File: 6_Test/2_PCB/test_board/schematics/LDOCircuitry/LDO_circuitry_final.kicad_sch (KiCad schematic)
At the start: 6 parts

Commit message: Edits 112524
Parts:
- removed C? (x2): 4.7uF, symbol Device:C
- removed C?: 100nF, symbol Device:C
- removed R?: 4.7k, symbol Device:R_US
- added C35, C36: 4.7u, Cap4.7uFFootprints:CAP_0603_CL10A_1P6XP8_SAM, symbol Device:C
- added C37: 100n, cap100nFFootprints:CAP_CL05_SAM, symbol Device:C
- added R32: 4.7k, ECE628_lib:resistor4.7k, symbol Device:R_US
- R?: value 6k -> 4.7k; footprint (none) -> ECE628_lib:resistor4.7k
- R?: footprint POT_PV37W_MUR -> ECE628_lib:potentiometer_10turn
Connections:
- net AVSS: now also C35.2, C36.2, C37.2, R32.2
- net VLDO: now also C36.1, C37.1
- net VREF: now also C35.1
- net at R?.1: now also R32.1
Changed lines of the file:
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@@
+	)
+	(symbol
+		(lib_id "Device:R_US")
+		(at 114.3 109.22 0)
+		(mirror y)
+		(unit 1)
+		(exclude_from_sim no)
+		(in_bom yes)
+		(on_board yes)
+		(dnp no)
+		(property "Reference" "R32"
+			(at 111.76 107.9499 0)
+			(effects
+				(font
+					(size 1.27 1.27)
+				)
+				(justify left)
+			)
+		)
+		(property "Value" "4.7k"
+			(at 111.76 110.4899 0)
+			(effects
+				(font
+					(size 1.27 1.27)
+				)
+				(justify left)
+			)
+		)
+		(property "Footprint" "ECE628_lib:resistor4.7k"
+			(at 113.284 109.474 90)
+			(effects
+				(font
+					(size 1.27 1.27)
+				)
+				(hide yes)
+			)
+		)
+		(property "Datasheet" "~"
+			(at 114.3 109.22 0)
+			(effects
+				(font
+					(size 1.27 1.27)
+				)
+				(hide yes)
+			)
+		)
+		(property "Description" "Resistor, US symbol"
+			(at 114.3 109.22 0)
+			(effects
+				(font
+					(size 1.27 1.27)
+				)
+				(hide yes)
+			)
+		)
+		(pin "2"
+		)
+		(pin "1"
+		)
+		(instances
+			(project "board_main"
+				(path "/9c0580c5-7bd5-4e54-bf4c-826aa4ac3630/104c40d7-ae25-447b-8675-a765b7f78bca"
+					(reference "R32")
+					(unit 1)
+				)
+			)
+		)
 	)
 	(symbol
 		(lib_id "Device:C")
-		(at 138.43 110.49 0)
-		(unit 1)
-		(exclude_from_sim no)
-		(in_bom yes)
-		(on_board yes)
-		(dnp no)
-		(property "Reference" "C?"
-			(at 143.764 111.506 0)
-			(effects
-				(font
-					(size 1.27 1.27)
-				)
-			)
-		)
-		(property "Value" "4.7uF"
-			(at 144.018 109.474 0)
-			(effects
-				(font
-					(size 1.27 1.27)
-				)
-			)
-		)
-		(property "Footprint" ""
-			(at 139.3952 114.3 0)
+		(at 149.86 110.49 0)
+		(unit 1)
+		(exclude_from_sim no)
+		(in_bom yes)
+		(on_board yes)
+		(dnp no)
+		(fields_autoplaced yes)
+		(property "Reference" "C37"
+			(at 153.67 109.2199 0)
+			(effects
+				(font
+					(size 1.27 1.27)
+				)
+				(justify left)
+			)
+		)
+		(property "Value" "100n"
+			(at 153.67 111.7599 0)
+			(effects
+				(font
+					(size 1.27 1.27)
+				)
+				(justify left)
+			)
+		)
+		(property "Footprint" "cap100nFFootprints:CAP_CL05_SAM"
+			(at 150.8252 114.3 0)
 			(effects
 				(font
@@
 		)
 		(property "Datasheet" "~"
-			(at 138.43 110.49 0)
+			(at 149.86 110.49 0)
 			(effects
 				(font
@@
 		)
 		(property "Description" "Unpolarized capacitor"
-			(at 138.43 110.49 0)
-			(effects
-				(font
-					(size 1.27 1.27)
-				)
-				(hide yes)
-			)
-		)
-		(pin "2"
-		)
-		(pin "1"
-		)
-		(instances
-			(project "LDO_circuitry_final"
-				(path "/1d203505-0113-4179-87e1-d4f3bd3291d4"
-					(reference "C?")
-					(unit 1)
-				)
-			)
-			(project "LDO_circuitry_final"
-				(path "/9c0580c5-7bd5-4e54-bf4c-826aa4ac3630/104c40d7-ae25-447b-8675-a765b7f78bca"
-					(reference "C?")
+			(at 149.86 110.49 0)
+			(effects
+				(font
+					(size 1.27 1.27)
+				)
+				(hide yes)
+			)
+		)
+		(pin "2"
+		)
+		(pin "1"
+		)
+		(instances
+			(project "board_main"
+				(path "/9c0580c5-7bd5-4e54-bf4c-826aa4ac3630/104c40d7-ae25-447b-8675-a765b7f78bca"
+					(reference "C37")
 					(unit 1)
 				)
@@
 			)
 		)
-		(property "Value" "6k"
+		(property "Value" "4.7k"
 			(at 111.76 82.5499 0)
 			(effects
@@
 			)
 		)
-		(property "Footprint" ""
+		(property "Footprint" "ECE628_lib:resistor4.7k"
 			(at 113.284 81.534 90)
 			(effects
@@
 				)
 			)
-			(project "LDO_circuitry_final"
-				(path "/9c0580c5-7bd5-4e54-bf4c-826aa4ac3630/104c40d7-ae25-447b-8675-a765b7f78bca"
-					(reference "R?")
-					(unit 1)
-				)
-			)
-		)
-	)
-	(symbol
-		(lib_id "Device:C")
-		(at 149.86 110.49 0)
-		(unit 1)
-		(exclude_from_sim no)
-		(in_bom yes)
-		(on_board yes)
-		(dnp no)
-		(property "Reference" "C?"
-			(at 155.448 111.506 0)
-			(effects
-				(font
-					(size 1.27 1.27)
-				)
-			)
-		)
-		(property "Value" "100nF"
-			(at 155.702 109.474 0)
-			(effects
-				(font
-					(size 1.27 1.27)
-				)
-			)
-		)
-		(property "Footprint" ""
-			(at 150.8252 114.3 0)
-			(effects
-				(font
-					(size 1.27 1.27)
-				)
-				(hide yes)
-			)
-		)
-		(property "Datasheet" "~"
-			(at 149.86 110.49 0)
-			(effects
-				(font
-					(size 1.27 1.27)
-				)
-				(hide yes)
-			)
-		)
-		(property "Description" "Unpolarized capacitor"
-			(at 149.86 110.49 0)
-			(effects
-				(font
-					(size 1.27 1.27)
-				)
-				(hide yes)
-			)
-		)
-		(pin "2"
-		)
-		(pin "1"
-		)
-		(instances
-			(project "LDO_circuitry_final"
-				(path "/1d203505-0113-4179-87e1-d4f3bd3291d4"
-					(reference "C?")
-					(unit 1)
-				)
-			)
-			(project "LDO_circuitry_final"
-				(path "/9c0580c5-7bd5-4e54-bf4c-826aa4ac3630/104c40d7-ae25-447b-8675-a765b7f78bca"
-					(reference "C?")
+			(project "board_main"
+				(path "/9c0580c5-7bd5-4e54-bf4c-826aa4ac3630/104c40d7-ae25-447b-8675-a765b7f78bca"
+					(reference "R30")
 					(unit 1)
 				)
@@
 		(on_board yes)
 		(dnp no)
-		(fields_autoplaced yes)
-		(property "Reference" "C?"
-			(at 127 102.8699 0)
-			(effects
-				(font
-					(size 1.27 1.27)
-				)
-				(justify left)
-			)
-		)
-		(property "Value" "4.7uF"
-			(at 127 105.4099 0)
-			(effects
-				(font
-					(size 1.27 1.27)
-				)
-				(justify left)
-			)
-		)
-		(property "Footprint" ""
+		(property "Reference" "C35"
+			(at 125.984 102.616 0)
+			(effects
+				(font
+					(size 1.27 1.27)
+				)
+				(justify left)
+			)
+		)
+		(property "Value" "4.7u"
+			(at 125.984 104.902 0)
+			(effects
+				(font
+					(size 1.27 1.27)
+				)
+				(justify left)
+			)
+		)
+		(property "Footprint" "Cap4.7uFFootprints:CAP_0603_CL10A_1P6XP8_SAM"
 			(at 124.1552 107.95 0)
 			(effects
@@
 		)
 		(instances
-			(project "LDO_circuitry_final"
-				(path "/1d203505-0113-4179-87e1-d4f3bd3291d4"
-					(reference "C?")
-					(unit 1)
-				)
-			)
-			(project "LDO_circuitry_final"
-				(path "/9c0580c5-7bd5-4e54-bf4c-826aa4ac3630/104c40d7-ae25-447b-8675-a765b7f78bca"
-					(reference "C?")
+			(project "board_main"
+				(path "/9c0580c5-7bd5-4e54-bf4c-826aa4ac3630/104c40d7-ae25-447b-8675-a765b7f78bca"
+					(reference "C35")
 					(unit 1)
 				)
@@
 			)
 		)
-		(property "Footprint" "POT_PV37W_MUR"
+		(property "Footprint" "ECE628_lib:potentiometer_10turn"
 			(at 114.3 105.41 0)
 			(effects
@@
 				)
 			)
-			(project "LDO_circuitry_final"
-				(path "/9c0580c5-7bd5-4e54-bf4c-826aa4ac3630/104c40d7-ae25-447b-8675-a765b7f78bca"
-					(reference "R?")
-					(unit 1)
-				)
-			)
-		)
-	)
-	(symbol
-		(lib_id "Device:R_US")
-		(at 114.3 109.22 0)
-		(mirror y)
-		(unit 1)
-		(exclude_from_sim no)
-		(in_bom yes)
-		(on_board yes)
-		(dnp no)
-		(property "Reference" "R?"
-			(at 111.76 107.9499 0)
-			(effects
-				(font
-					(size 1.27 1.27)
-				)
-				(justify left)
-			)
-		)
-		(property "Value" "4.7k"
-			(at 111.76 110.4899 0)
-			(effects
-				(font
-					(size 1.27 1.27)
-				)
-				(justify left)
-			)
-		)
-		(property "Footprint" ""
-			(at 113.284 109.474 90)
+			(project "board_main"
+				(path "/9c0580c5-7bd5-4e54-bf4c-826aa4ac3630/104c40d7-ae25-447b-8675-a765b7f78bca"
+					(reference "R31")
+					(unit 1)
+				)
+			)
+		)
+	)
+	(symbol
+		(lib_id "Device:C")
+		(at 138.43 110.49 0)
+		(unit 1)
+		(exclude_from_sim no)
+		(in_bom yes)
+		(on_board yes)
+		(dnp no)
+		(property "Reference" "C36"
+			(at 141.224 108.966 0)
+			(effects
+				(font
+					(size 1.27 1.27)
+				)
+				(justify left)
+			)
+		)
+		(property "Value" "4.7u"
+			(at 141.224 111.252 0)
+			(effects
+				(font
+					(size 1.27 1.27)
+				)
+				(justify left)
+			)
+		)
+		(property "Footprint" "Cap4.7uFFootprints:CAP_0603_CL10A_1P6XP8_SAM"
+			(at 139.3952 114.3 0)
 			(effects
 				(font
@@
 		)
 		(property "Datasheet" "~"
-			(at 114.3 109.22 0)
-			(effects
-				(font
-					(size 1.27 1.27)
-				)
-				(hide yes)
-			)
-		)
-		(property "Description" "Resistor, US symbol"
-			(at 114.3 109.22 0)
-			(effects
-				(font
-					(size 1.27 1.27)
-				)
-				(hide yes)
-			)
-		)
-		(pin "2"
-		)
-		(pin "1"
-		)
-		(instances
-			(project "LDO_circuitry_final"
-				(path "/1d203505-0113-4179-87e1-d4f3bd3291d4"
-					(reference "R?")
-					(unit 1)
-				)
-			)
-			(project "LDO_circuitry_final"
-				(path "/9c0580c5-7bd5-4e54-bf4c-826aa4ac3630/104c40d7-ae25-447b-8675-a765b7f78bca"
-					(reference "R?")
-					(unit 1)
-				)
+			(at 138.43 110.49 0)
+			(effects
+				(font
+					(size 1.27 1.27)
+				)
+				(hide yes)
+			)
+		)
+		(property "Description" "Unpolarized capacitor"
+			(at 138.43 110.49 0)
+			(effects
+				(font
+					(size 1.27 1.27)
+				)
+				(hide yes)
+			)
+		)
+		(pin "2"
+		)
+		(pin "1"
+		)
+		(instances
+			(project "board_main"
+				(path "/9c0580c5-7bd5-4e54-bf4c-826aa4ac3630/104c40d7-ae25-447b-8675-a765b7f78bca"
+					(reference "C36")
+					(unit 1)
+				)

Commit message: final draft of board, revision 2
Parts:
- C35, C36: footprint Cap4.7uFFootprints:CAP_0603_CL10A_1P6XP8_SAM -> Capacitor_SMD:C_0603_1608Metric
- C37: footprint cap100nFFootprints:CAP_CL05_SAM -> Capacitor_SMD:C_0402_1005Metric
- R32, R?: footprint ECE628_lib:resistor4.7k -> Resistor_SMD:R_0402_1005Metric
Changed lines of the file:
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@@
 			)
 		)
-		(property "Footprint" "ECE628_lib:resistor4.7k"
+		(property "Footprint" "Resistor_SMD:R_0402_1005Metric"
 			(at 113.284 109.474 90)
 			(effects
@@
 			)
 		)
-		(property "Footprint" "cap100nFFootprints:CAP_CL05_SAM"
+		(property "Footprint" "Capacitor_SMD:C_0402_1005Metric"
 			(at 150.8252 114.3 0)
 			(effects
@@
 			)
 		)
-		(property "Footprint" "ECE628_lib:resistor4.7k"
+		(property "Footprint" "Resistor_SMD:R_0402_1005Metric"
 			(at 113.284 81.534 90)
 			(effects
@@
 			)
 		)
-		(property "Footprint" "Cap4.7uFFootprints:CAP_0603_CL10A_1P6XP8_SAM"
+		(property "Footprint" "Capacitor_SMD:C_0603_1608Metric"
 			(at 124.1552 107.95 0)
 			(effects
@@
 			)
 		)
-		(property "Footprint" "Cap4.7uFFootprints:CAP_0603_CL10A_1P6XP8_SAM"
+		(property "Footprint" "Capacitor_SMD:C_0603_1608Metric"
 			(at 139.3952 114.3 0)
 			(effects

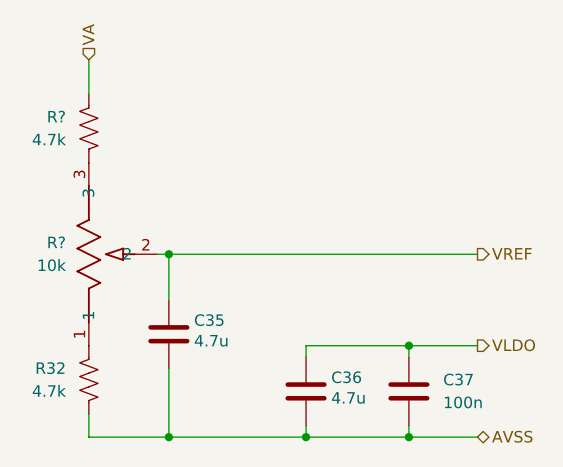
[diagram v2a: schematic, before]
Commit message: Edit Layout 1_27
Rearranged the components in the layout and added majority of traces and ground layer. AVSS connections still need to be connected along with IOVDD
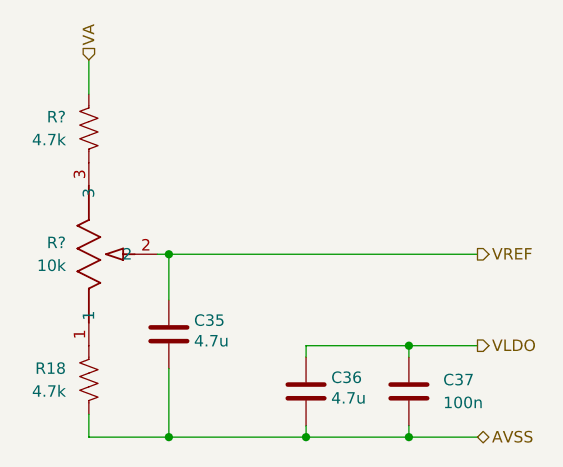
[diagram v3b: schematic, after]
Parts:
- renumbered R32 to R18
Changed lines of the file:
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@@
 		(on_board yes)
 		(dnp no)
-		(property "Reference" "R32"
+		(property "Reference" "R18"
 			(at 111.76 107.9499 0)
 			(effects
@@
 			(project "board_main"
 				(path "/9c0580c5-7bd5-4e54-bf4c-826aa4ac3630/104c40d7-ae25-447b-8675-a765b7f78bca"
-					(reference "R32")
+					(reference "R18")
 					(unit 1)
 				)
@@
 			(project "board_main"
 				(path "/9c0580c5-7bd5-4e54-bf4c-826aa4ac3630/104c40d7-ae25-447b-8675-a765b7f78bca"
-					(reference "R30")
+					(reference "R16")
 					(unit 1)
 				)
@@
 			(project "board_main"
 				(path "/9c0580c5-7bd5-4e54-bf4c-826aa4ac3630/104c40d7-ae25-447b-8675-a765b7f78bca"
-					(reference "R31")
-					(unit 1)
-				)
+					(reference "R17")
+					(unit 1)
+				)
